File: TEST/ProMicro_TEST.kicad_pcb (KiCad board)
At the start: 2 copper layers, 17.8 x 30.5 mm, 6 parts

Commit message: route
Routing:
- net +3V3: track 0.00 -> 18.8 mm
- net SDA: track 0.00 -> 2.06 mm
- net SCL: track 0.00 -> 2.03 mm
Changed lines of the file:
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@@
     (thickness 0.8)
     (drawings 67)
-    (tracks 0)
+    (tracks 14)
     (zones 0)
     (modules 6)
@@
     (uvia_dia 0.3)
     (uvia_drill 0.1)
-    (add_net +5V)
-    (add_net BTN)
-    (add_net CIPO)
-    (add_net COPI)
-    (add_net CS0)
-    (add_net CS1)
-    (add_net D8)
-    (add_net INT)
-    (add_net PWM)
-    (add_net RXD)
-    (add_net SCK)
     (add_net SCL)
     (add_net SDA)
-    (add_net STAT)
-    (add_net TCK)
-    (add_net TDI)
-    (add_net TDO)
-    (add_net TMS)
-    (add_net TXD)
-    (add_net ~RST)
   )
   (net_class Power ""
@@
   (gr_line (start 153.035 115.57) (end 136.525 115.57) (layer Edge.Cuts) (width 0.1))
   (gr_line (start 136.525 85.09) (end 153.035 85.09) (layer Edge.Cuts) (width 0.1))
+  (segment (start 146.685 107.465) (end 146.685 106.68) (width 0.4) (layer B.Cu) (net 2))
+  (segment (start 146.685 106.68) (end 147.32 106.68) (width 0.4) (layer B.Cu) (net 2))
+  (segment (start 137.16 106.68) (end 146.685 106.68) (width 0.4) (layer B.Cu) (net 2))
+  (segment (start 148.59 105.41) (end 148.717 105.283) (width 0.4) (layer B.Cu) (net 2))
+  (segment (start 148.59 107.1625) (end 148.59 105.41) (width 0.4) (layer B.Cu) (net 2))
+  (segment (start 147.32 106.68) (end 148.717 105.283) (width 0.4) (layer B.Cu) (net 2))
+  (segment (start 149.225 104.775) (end 148.717 105.283) (width 0.4) (layer B.Cu) (net 2))
+  (segment (start 149.375 104.625) (end 149.225 104.775) (width 0.4) (layer B.Cu) (net 2))
+  (segment (start 149.375 104.14) (end 149.375 104.625) (width 0.4) (layer B.Cu) (net 2))
+  (segment (start 149.375 104.14) (end 149.375 102.72) (width 0.4) (layer B.Cu) (net 2))
+  (segment (start 149.375 101.6) (end 149.375 102.72) (width 0.4) (layer B.Cu) (net 2))
+  (segment (start 152.4 101.6) (end 150.368 101.6) (width 0.25) (layer B.Cu) (net 3))
+  (segment (start 150.345 104.14) (end 150.749 104.14) (width 0.25) (layer B.Cu) (net 4))
+  (segment (start 152.4 104.14) (end 150.749 104.14) (width 0.25) (layer B.Cu) (net 4))
   (zone (net 1) (net_name GND) (layer F.Cu) (hatch edge 0.508)
     (connect_pads (clearance 0.125))

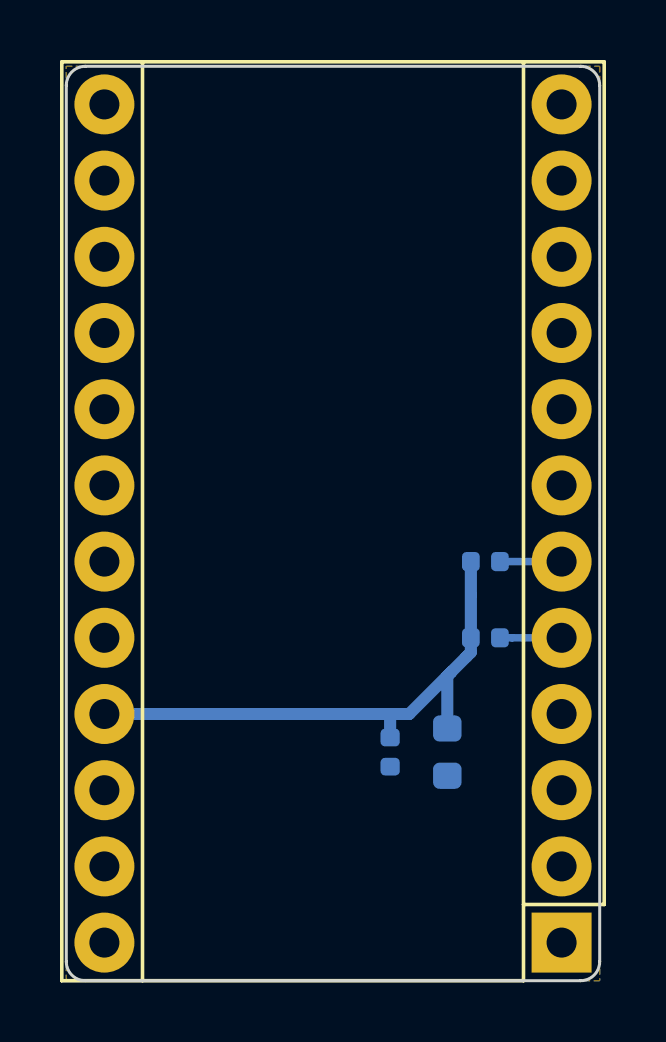
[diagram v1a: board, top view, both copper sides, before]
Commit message: make controller holes wide enough
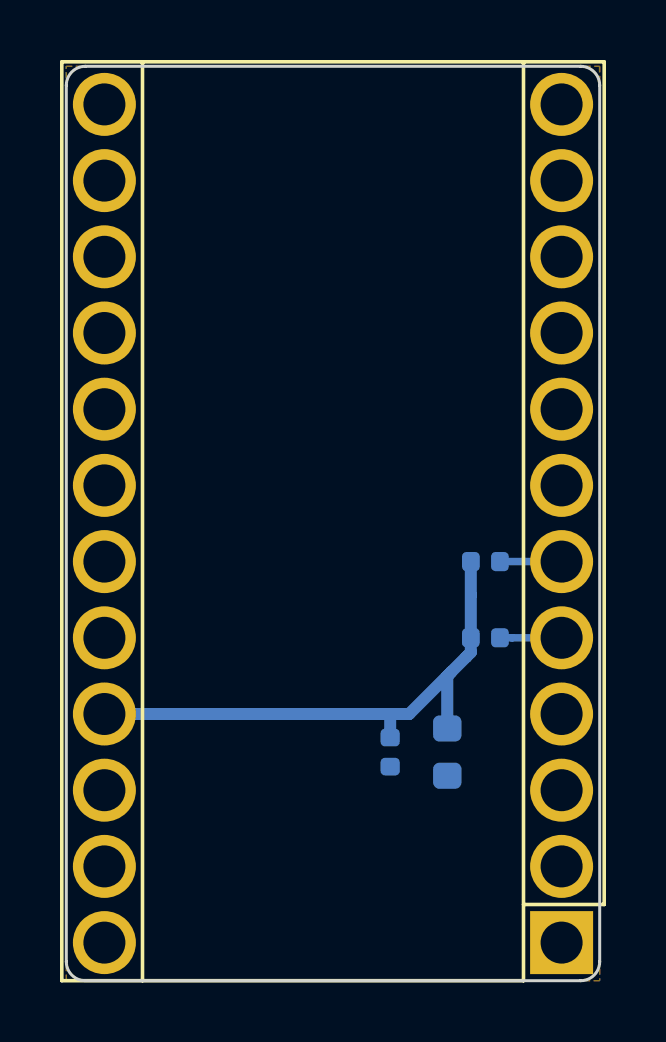
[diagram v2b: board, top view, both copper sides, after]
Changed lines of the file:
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@@
-(kicad_pcb (version 20171130) (host pcbnew 5.1.5+dfsg1-2build2)
+(kicad_pcb (version 20171130) (host pcbnew 5.1.5)
   (general
     (thickness 0.8)
@@
       (effects (font (size 1 1) (thickness 0.15)))
     )
-    (pad 1 thru_hole rect (at 0 0 180) (size 2 2) (drill 1) (layers *.Cu *.Mask))
-    (pad 2 thru_hole oval (at 0 2.54 180) (size 2 2) (drill 1) (layers *.Cu *.Mask))
-    (pad 3 thru_hole oval (at 0 5.08 180) (size 2 2) (drill 1) (layers *.Cu *.Mask)
+    (pad 1 thru_hole rect (at 0 0 180) (size 2.1 2.1) (drill 1.4) (layers *.Cu *.Mask))
+    (pad 2 thru_hole circle (at 0 2.54 180) (size 2.1 2.1) (drill 1.4) (layers *.Cu *.Mask))
+    (pad 3 thru_hole circle (at 0 5.08 180) (size 2.1 2.1) (drill 1.4) (layers *.Cu *.Mask)
       (net 1 GND))
-    (pad 13 thru_hole oval (at 15.24 27.94 180) (size 2 2) (drill 1) (layers *.Cu *.Mask))
-    (pad 4 thru_hole oval (at 0 7.62 180) (size 2 2) (drill 1) (layers *.Cu *.Mask)
+    (pad 13 thru_hole circle (at 15.24 27.94 180) (size 2.1 2.1) (drill 1.4) (layers *.Cu *.Mask))
+    (pad 4 thru_hole circle (at 0 7.62 180) (size 2.1 2.1) (drill 1.4) (layers *.Cu *.Mask)
       (net 1 GND))
-    (pad 14 thru_hole oval (at 15.24 25.4 180) (size 2 2) (drill 1) (layers *.Cu *.Mask))
-    (pad 5 thru_hole oval (at 0 10.16 180) (size 2 2) (drill 1) (layers *.Cu *.Mask)
+    (pad 14 thru_hole circle (at 15.24 25.4 180) (size 2.1 2.1) (drill 1.4) (layers *.Cu *.Mask))
+    (pad 5 thru_hole circle (at 0 10.16 180) (size 2.1 2.1) (drill 1.4) (layers *.Cu *.Mask)
       (net 4 SDA))
-    (pad 15 thru_hole oval (at 15.24 22.86 180) (size 2 2) (drill 1) (layers *.Cu *.Mask))
-    (pad 6 thru_hole oval (at 0 12.7 180) (size 2 2) (drill 1) (layers *.Cu *.Mask)
+    (pad 15 thru_hole circle (at 15.24 22.86 180) (size 2.1 2.1) (drill 1.4) (layers *.Cu *.Mask))
+    (pad 6 thru_hole circle (at 0 12.7 180) (size 2.1 2.1) (drill 1.4) (layers *.Cu *.Mask)
       (net 3 SCL))
-    (pad 16 thru_hole oval (at 15.24 20.32 180) (size 2 2) (drill 1) (layers *.Cu *.Mask))
-    (pad 7 thru_hole oval (at 0 15.24 180) (size 2 2) (drill 1) (layers *.Cu *.Mask))
-    (pad 17 thru_hole oval (at 15.24 17.78 180) (size 2 2) (drill 1) (layers *.Cu *.Mask))
-    (pad 8 thru_hole oval (at 0 17.78 180) (size 2 2) (drill 1) (layers *.Cu *.Mask))
-    (pad 18 thru_hole oval (at 15.24 15.24 180) (size 2 2) (drill 1) (layers *.Cu *.Mask))
-    (pad 9 thru_hole oval (at 0 20.32 180) (size 2 2) (drill 1) (layers *.Cu *.Mask))
-    (pad 19 thru_hole oval (at 15.24 12.7 180) (size 2 2) (drill 1) (layers *.Cu *.Mask))
-    (pad 10 thru_hole oval (at 0 22.86 180) (size 2 2) (drill 1) (layers *.Cu *.Mask))
-    (pad 20 thru_hole oval (at 15.24 10.16 180) (size 2 2) (drill 1) (layers *.Cu *.Mask))
-    (pad 11 thru_hole oval (at 0 25.4 180) (size 2 2) (drill 1) (layers *.Cu *.Mask))
-    (pad 21 thru_hole oval (at 15.24 7.62 180) (size 2 2) (drill 1) (layers *.Cu *.Mask)
+    (pad 16 thru_hole circle (at 15.24 20.32 180) (size 2.1 2.1) (drill 1.4) (layers *.Cu *.Mask))
+    (pad 7 thru_hole circle (at 0 15.24 180) (size 2.1 2.1) (drill 1.4) (layers *.Cu *.Mask))
+    (pad 17 thru_hole circle (at 15.24 17.78 180) (size 2.1 2.1) (drill 1.4) (layers *.Cu *.Mask))
+    (pad 8 thru_hole circle (at 0 17.78 180) (size 2.1 2.1) (drill 1.4) (layers *.Cu *.Mask))
+    (pad 18 thru_hole circle (at 15.24 15.24 180) (size 2.1 2.1) (drill 1.4) (layers *.Cu *.Mask))
+    (pad 9 thru_hole circle (at 0 20.32 180) (size 2.1 2.1) (drill 1.4) (layers *.Cu *.Mask))
+    (pad 19 thru_hole circle (at 15.24 12.7 180) (size 2.1 2.1) (drill 1.4) (layers *.Cu *.Mask))
+    (pad 10 thru_hole circle (at 0 22.86 180) (size 2.1 2.1) (drill 1.4) (layers *.Cu *.Mask))
+    (pad 20 thru_hole circle (at 15.24 10.16 180) (size 2.1 2.1) (drill 1.4) (layers *.Cu *.Mask))
+    (pad 11 thru_hole circle (at 0 25.4 180) (size 2.1 2.1) (drill 1.4) (layers *.Cu *.Mask))
+    (pad 21 thru_hole circle (at 15.24 7.62 180) (size 2.1 2.1) (drill 1.4) (layers *.Cu *.Mask)
       (net 2 +3V3))
-    (pad 12 thru_hole oval (at 0 27.94 180) (size 2 2) (drill 1) (layers *.Cu *.Mask))
-    (pad 22 thru_hole oval (at 15.24 5.08 180) (size 2 2) (drill 1) (layers *.Cu *.Mask))
-    (pad 23 thru_hole oval (at 15.24 2.54 180) (size 2 2) (drill 1) (layers *.Cu *.Mask)
+    (pad 12 thru_hole circle (at 0 27.94 180) (size 2.1 2.1) (drill 1.4) (layers *.Cu *.Mask))
+    (pad 22 thru_hole circle (at 15.24 5.08 180) (size 2.1 2.1) (drill 1.4) (layers *.Cu *.Mask))
+    (pad 23 thru_hole circle (at 15.24 2.54 180) (size 2.1 2.1) (drill 1.4) (layers *.Cu *.Mask)
       (net 1 GND))
-    (pad 24 thru_hole oval (at 15.24 0 180) (size 2 2) (drill 1) (layers *.Cu *.Mask))
+    (pad 24 thru_hole circle (at 15.24 0 180) (size 2.1 2.1) (drill 1.4) (layers *.Cu *.Mask))
     (model ${KISYS3DMOD}/Module.3dshapes/Sparkfun_Pro_Micro.wrl
       (at (xyz 0 0 0))
